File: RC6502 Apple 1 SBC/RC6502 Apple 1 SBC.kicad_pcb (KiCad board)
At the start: 2 copper layers, 99.1 x 99.7 mm, 46 parts, among them J1 VP GND, J10 RAM_EN, J2 Arduino Nano, J3 Backplane, J4 Hole, J5 Hole, J6 Hole, J7 Hole, J8 Power, J9 ROM_EN, SW1 RESET, U1 WD65C02, U2 HM62256BLP-7, U3 74HCT138, U4 28C256, U5 74HCT00, U6 NE555, U7 74HCT04, U8 WD65C21, U9 MCP23S17, X1 1MHz

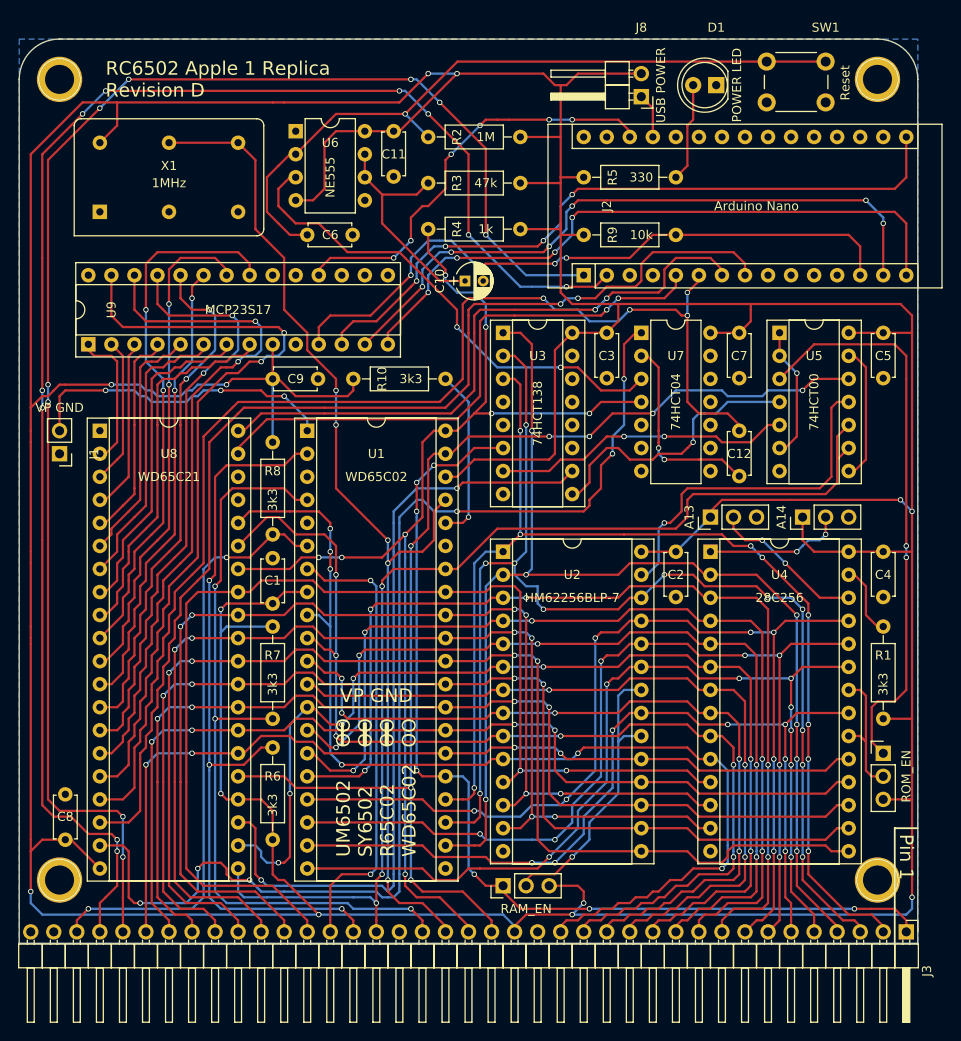
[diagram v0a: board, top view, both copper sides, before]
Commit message: Added PIA enable jumper to SBC
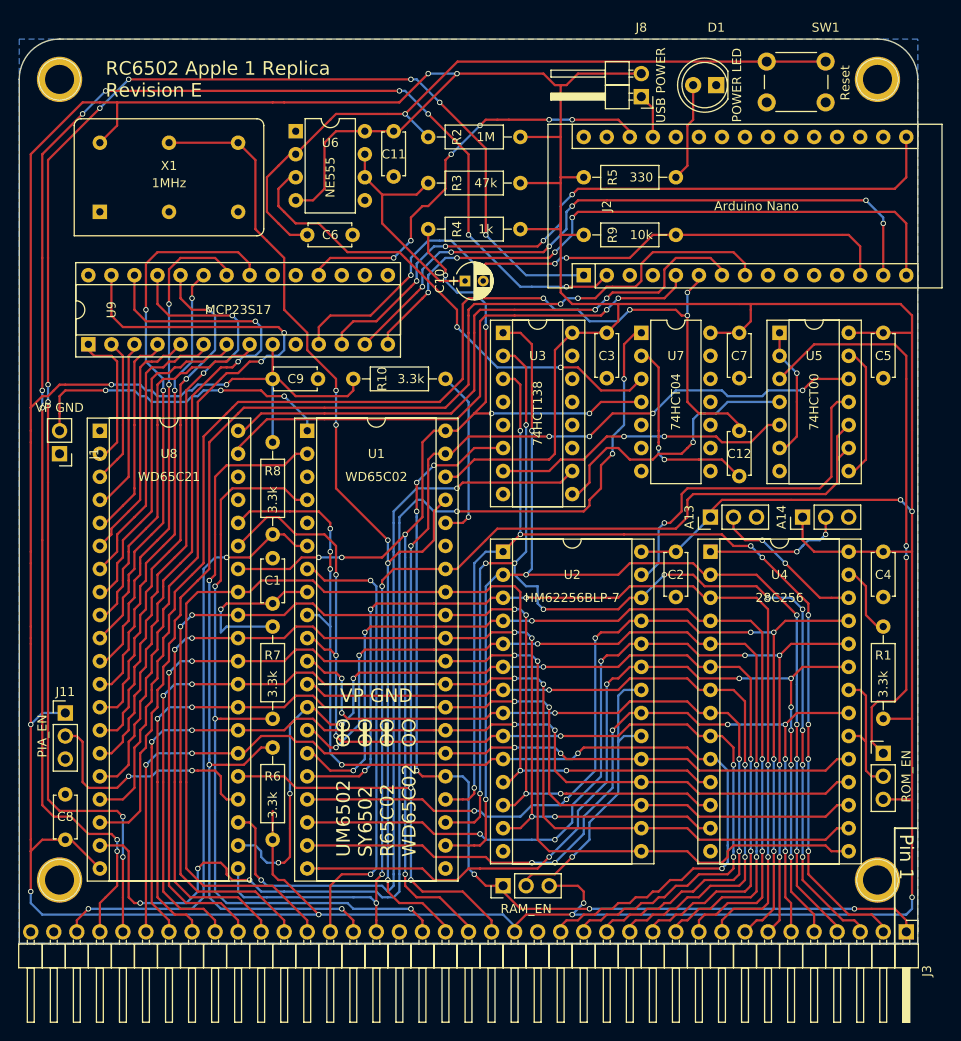
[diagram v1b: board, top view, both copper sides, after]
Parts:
- added J11: PIA_EN, Pin_Headers:Pin_Header_Straight_1x03_Pitch2.54mm, F.Cu at (121.3, 113.7)
- R1, R10, R6, R7, R8: value 3k3 -> 3.3k
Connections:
- U8 pad 24: VCC -> Net-(J11-Pad2)
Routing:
- net Net-(J11-Pad2): track 0.00 -> 27.2 mm, vias 0 -> 2
- net VCC: track 661.0 -> 641.0 mm
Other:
- board text added: "PIA_EN"
- board text added: "RC6502 Apple 1 Replica Revision E"
- board text removed: "RC6502 Apple 1 Replica Revision D"

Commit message: Added oscillator enable jumper to SBC
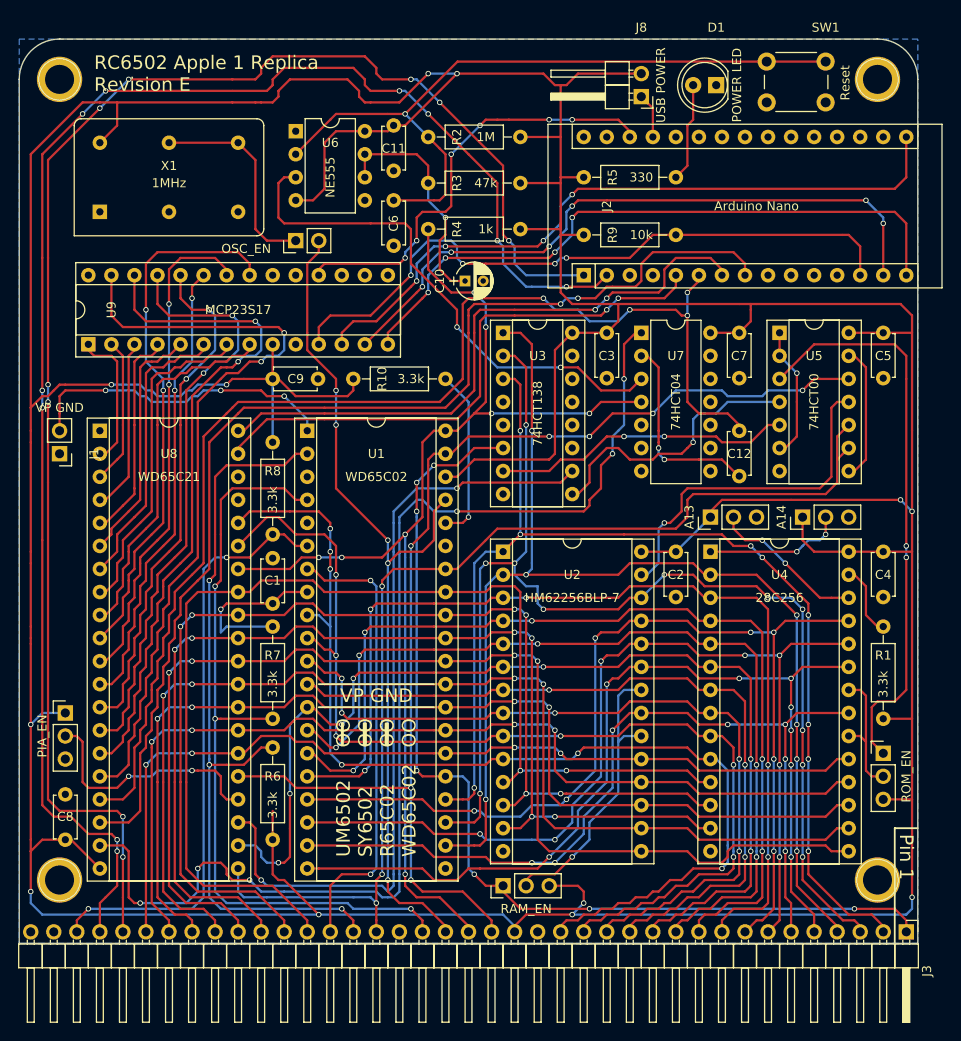
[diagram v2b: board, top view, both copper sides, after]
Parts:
- added JP1: OSC_EN, Pin_Headers:Pin_Header_Straight_1x02_Pitch2.54mm, F.Cu at (146.7, 61.6)
- moved C6 10.3 mm to (157.5, 57.1), turned to 270 degrees
- moved C11 0.63 mm to (157.5, 48.9)
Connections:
- X1 pad 8: CLOCK -> Net-(JP1-Pad1)
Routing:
- net Net-(JP1-Pad1): track 0.00 -> 22.9 mm
- net CLOCK: track 116.7 -> 95.6 mm
- net Net-(U6-Pad3): track 54.4 -> 57.7 mm
- net VCC: track 641.0 -> 643.9 mm
- net TX: track 169.5 -> 172.3 mm
- net RX: track 172.3 -> 174.8 mm
- net P_RESET: track 46.3 -> 48.1 mm
- net Net-(C6-Pad1): track 79.8 -> 80.6 mm
- net Net-(C10-Pad1): track 25.8 -> 26.2 mm, vias 0 -> 1
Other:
- board text added: "OSC_EN"

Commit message: Updated gerbers for order
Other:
- board text added: "VP_GND"
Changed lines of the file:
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@@
     (links 240)
     (no_connects 1)
-    (area 116.129999 39.294999 215.340001 139.140001)
+    (area 114.23 35.22 220.820001 148.420001)
     (thickness 1.6)
-    (drawings 162)
+    (drawings 168)
     (tracks 2242)
     (zones 0)
@@
     )
   )
+  (gr_text VP_GND (at 118.11 83.82 90) (layer B.SilkS)
+    (effects (font (size 1 1) (thickness 0.1)) (justify mirror))
+  )
+  (gr_line (start 120.65 82.55) (end 120.65 85.09) (angle 90) (layer B.SilkS) (width 0.2))
+  (gr_line (start 118.745 86.995) (end 118.745 80.645) (angle 90) (layer B.SilkS) (width 0.2))
+  (gr_line (start 122.555 86.995) (end 118.745 86.995) (angle 90) (layer B.SilkS) (width 0.2))
+  (gr_line (start 122.555 80.645) (end 122.555 86.995) (angle 90) (layer B.SilkS) (width 0.2))
+  (gr_line (start 118.745 80.645) (end 122.555 80.645) (angle 90) (layer B.SilkS) (width 0.2))
   (gr_text OSC_EN (at 144.145 62.865) (layer B.SilkS)
     (effects (font (size 1 1) (thickness 0.1)) (justify left mirror))
@@
   (gr_line (start 119.38 117.475) (end 119.38 111.76) (angle 90) (layer B.SilkS) (width 0.2))
   (gr_line (start 123.19 117.475) (end 119.38 117.475) (angle 90) (layer B.SilkS) (width 0.2))
-  (gr_text https://hvetebolle.blogspot.com (at 118.11 69.215 90) (layer B.SilkS)
-    (effects (font (size 1.5 1.5) (thickness 0.3)) (justify mirror))
+  (gr_text https://hvetebolle.blogspot.com (at 117.475 62.865 90) (layer B.SilkS)
+    (effects (font (size 1 1) (thickness 0.15)) (justify mirror))
   )
   (gr_line (start 169.545 132.715) (end 172.085 132.715) (angle 90) (layer B.SilkS) (width 0.2))
